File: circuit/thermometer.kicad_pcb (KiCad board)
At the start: 2 copper layers, 29 parts, among them IC1 ICL7107CPL, IC2 TMP36, IC3 LM285Z-1.2, IC4 4001, J1 Conn_01x25_Socket, J2 Conn_01x25_Pin

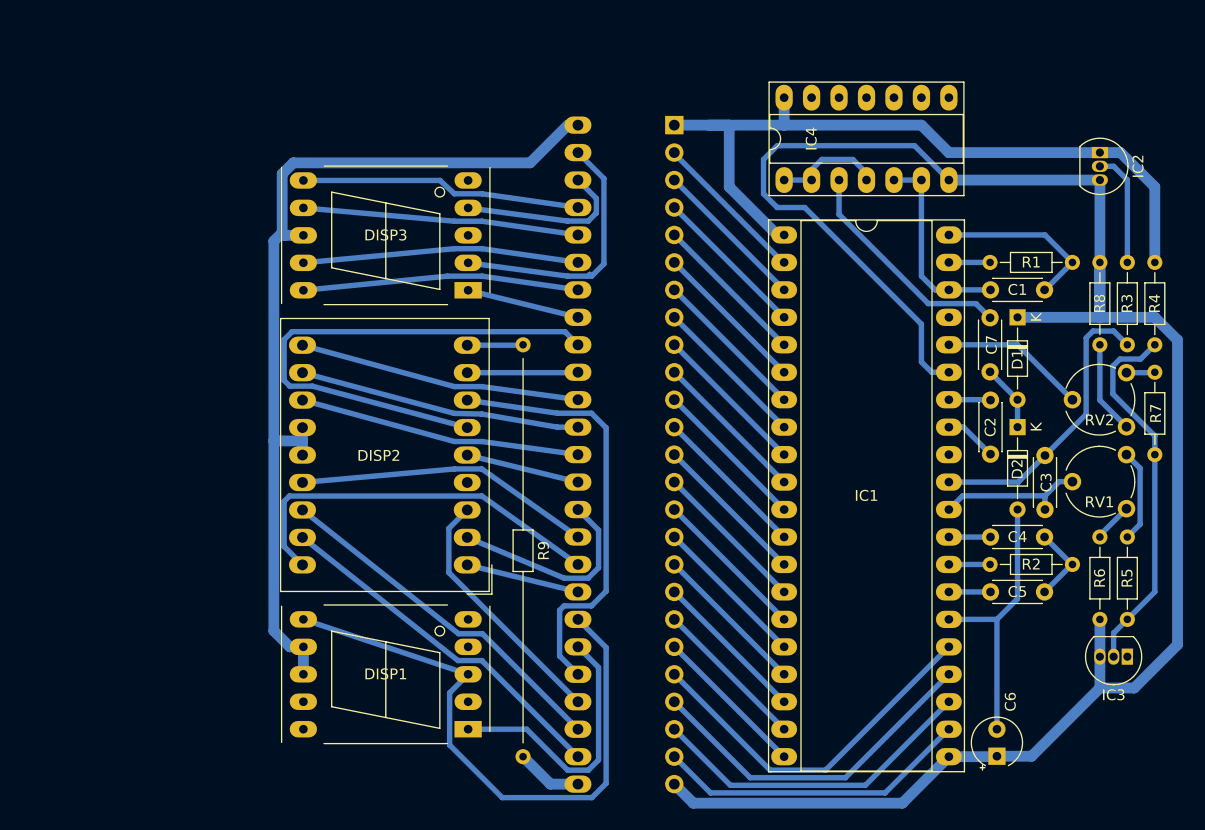
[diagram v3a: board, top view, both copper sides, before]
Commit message: PCB for the thermoboard module
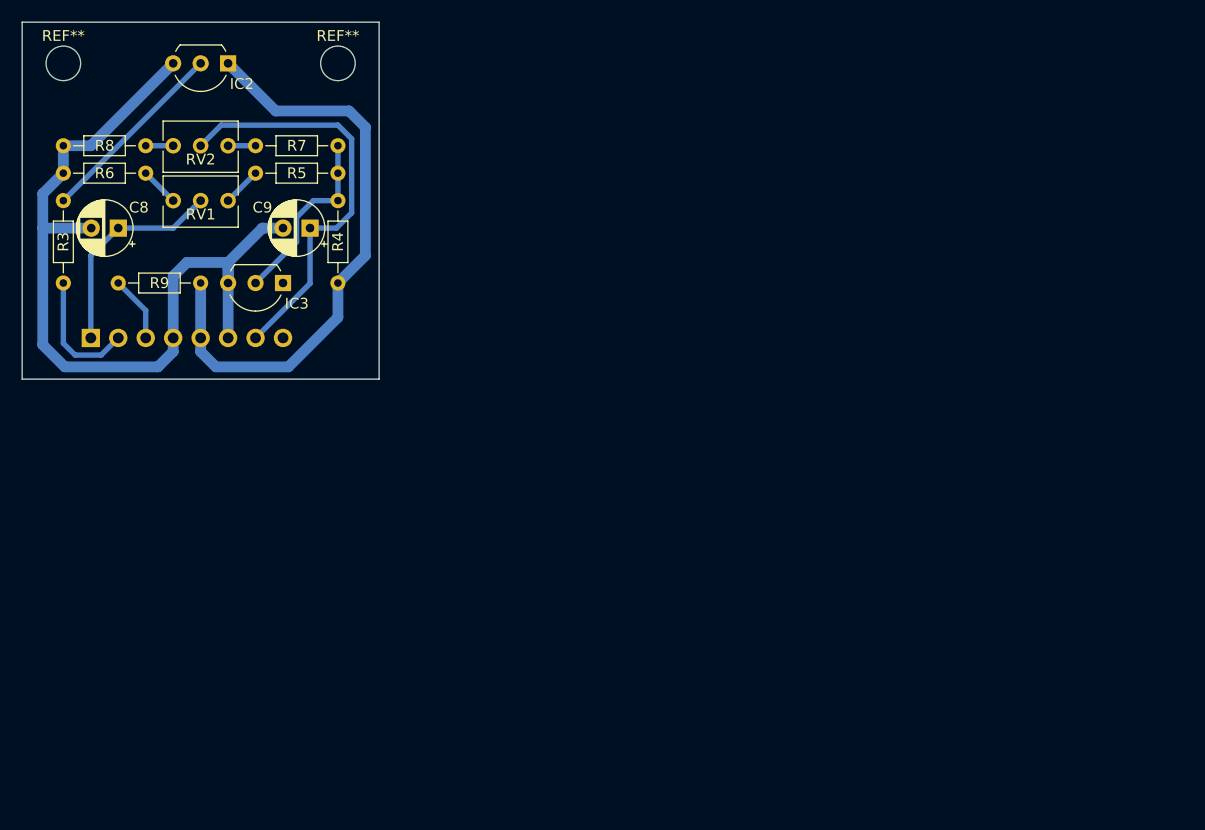
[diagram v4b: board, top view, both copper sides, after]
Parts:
- removed C1: 100pF, Capacitor_THT:C_Disc_D4.3mm_W1.9mm_P5.00mm
- removed C2: 100nF, Capacitor_THT:C_Disc_D4.3mm_W1.9mm_P5.00mm
- removed C3: 1uF, Capacitor_THT:C_Disc_D4.3mm_W1.9mm_P5.00mm
- removed C4: 470nF, Capacitor_THT:C_Disc_D4.3mm_W1.9mm_P5.00mm
- removed C5: 220nF, Capacitor_THT:C_Disc_D4.3mm_W1.9mm_P5.00mm
- removed C6: 10uF, Capacitor_THT:CP_Radial_Tantal_D4.5mm_P2.50mm
- removed C7: 47nF, Capacitor_THT:C_Disc_D4.3mm_W1.9mm_P5.00mm
- removed D1, D2: 1N4148, Diode_THT:D_DO-34_SOD68_P7.62mm_Horizontal
- removed DISP1: RS 587-967, Display_7Segment:7SegmentLED_LTS6760_LTS6780
- removed DISP2: D512HDB, Display_7Segment:DA56-11SURKWA
- removed DISP3: SA56-11HDB, Display_7Segment:7SegmentLED_LTS6760_LTS6780
- removed IC1: ICL7107CPL, Package_DIP:DIP-40_W15.24mm_Socket_LongPads
- removed IC4: 4001, Package_DIP:DIP-14_W7.62mm_Socket_LongPads
- removed J1: Conn_01x25_Socket, Connector_PinSocket_2.54mm:PinSocket_1x25_P2.54mm_Vertical
- removed R1: 100k, Resistor_THT:R_Axial_DIN0204_L3.6mm_D1.6mm_P7.62mm_Horizontal
- removed R2: 47k, Resistor_THT:R_Axial_DIN0204_L3.6mm_D1.6mm_P7.62mm_Horizontal
- added C8: 10uF, Capacitor_THT:CP_Radial_D5.0mm_P2.50mm, F.Cu at (72.4, 73.7)
- added C9: 10uF, Capacitor_THT:CP_Radial_D5.0mm_P2.50mm, F.Cu at (90.1, 73.7)
- added REF**: MountingHole_3.2mm_M3, MountingHole:MountingHole_3.2mm_M3, F.Cu at (67.3, 58.4)
- added REF**: MountingHole_3.2mm_M3, MountingHole:MountingHole_3.2mm_M3, F.Cu at (92.7, 58.4)
- IC2, IC3: footprint Package_TO_SOT_THT:TO-92_Inline -> Package_TO_SOT_THT:TO-92L_Inline_Wide
- J2: value Conn_01x25_Pin -> ~; footprint Connector_PinHeader_2.54mm:PinHeader_1x25_P2.54mm_Vertical -> Connector_PinHeader_2.54mm:PinHeader_1x08_P2.54mm_Vertical
- R3: value 1M -> 33k
- R9: value 620R -> 27k
- RV1, RV2: footprint Potentiometer_THT:Potentiometer_Piher_PT-6-V_Vertical -> Potentiometer_THT:Potentiometer_Bourns_3266Y_Vertical
- moved R3 98.6 mm to (67.3, 71.1)
- moved R6 94.5 mm to (74.9, 68.6), turned to 180 degrees
- moved R8 90.2 mm to (74.9, 66.0), turned to 180 degrees
- moved RV1 86.4 mm to (82.5, 71.1), turned to 0 degrees
- moved RV2 85.7 mm to (82.5, 66.0), turned to 0 degrees
- moved IC3 85.4 mm to (87.6, 78.7)
- moved R5 83.9 mm to (92.7, 68.6), turned to 180 degrees
- moved IC2 81.1 mm to (82.5, 58.4), turned to 180 degrees
- moved R7 80.8 mm to (92.7, 66.0), turned to 180 degrees
- moved R4 75.6 mm to (92.7, 78.7), turned to 90 degrees
- moved J2 49.2 mm to (69.8, 83.8), turned to -90 degrees
- moved R9 36.5 mm to (80.0, 78.7), turned to 180 degrees
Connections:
- IC2 pad 1: +5V -> Net-(IC2-+V_{S})
- IC2 pad 3: GND -> Net-(IC2-GND)
- IC3 pad 3: GND -> Net-(IC2-GND)
- J2 pad 1: Net-(DISP2-ca1) -> Net-(J2-Pin_1)
- J2 pad 2: Net-(DISP3-d) -> Net-(J2-Pin_2)
- J2 pad 3: Net-(DISP3-c) -> Net-(J2-Pin_3)
- J2 pad 4: Net-(DISP3-b) -> Net-(IC2-GND)
- J2 pad 5: Net-(DISP3-a) -> Net-(IC2-+V_{S})
- J2 pad 6: Net-(DISP3-f) -> Net-(IC2-GND)
- J2 pad 7: Net-(DISP3-g) -> Net-(J2-Pin_7)
- J2 pad 8: Net-(DISP3-e) -> unconnected-(J2-Pin_8-Pad8)
- R3 pad 2: Net-(IC1-IN_HI) -> Net-(J2-Pin_2)
- R4 pad 1: +5V -> Net-(IC2-+V_{S})
- R6 pad 2: GND -> Net-(IC2-GND)
- R8 pad 2: GND -> Net-(IC2-GND)
- R9 pad 1: Net-(DISP2-dp2) -> Net-(IC2-+V_{S})
- R9 pad 2: Net-(J2-Pin_25) -> Net-(J2-Pin_3)
- RV1 pad 2: Net-(IC1-IN_LO) -> Net-(J2-Pin_1)
- RV2 pad 2: Net-(IC1-REF_HI) -> Net-(J2-Pin_7)
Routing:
- net GND: track 182.9 -> 0.00 mm
- net Net-(DISP2-ca1): track 85.0 -> 0.00 mm
- net Net-(IC2-GND): track 0.00 -> 77.9 mm
- net +5V: track 70.9 -> 0.00 mm
- net Net-(DISP1-a): track 56.6 -> 0.00 mm
- net Net-(IC2-+V_{S}): track 0.00 -> 55.4 mm
- net Net-(DISP2-d2): track 49.4 -> 0.00 mm
- net Net-(DISP2-g2): track 40.3 -> 0.00 mm
- net Net-(J2-Pin_7): track 0.00 -> 38.8 mm
- net Net-(DISP2-f1): track 36.0 -> 0.00 mm
- net Net-(IC1-G2): track 33.8 -> 0.00 mm
- net Net-(DISP2-g1): track 33.1 -> 0.00 mm
- net Net-(DISP2-a1): track 33.1 -> 0.00 mm
- net Net-(IC1-C3): track 32.3 -> 0.00 mm
- net Net-(IC1-A3): track 30.8 -> 0.00 mm
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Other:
- board outline added: 33 x 33 mm
